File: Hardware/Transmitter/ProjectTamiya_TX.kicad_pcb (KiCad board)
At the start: 2 copper layers, 106.2 x 40 mm, 44 parts, among them J1 Boot, J10 NRF, J11 NRF_power, J2 Power, J3 Serial, J4 Steering, J5 Throttle, J6 ENC1, J7 OLED, J8 ENC2, J9 Debug, Q1 2N7002A, Q2 2N7002A, Q3 2N7002A, SW1 Reset, SW2 Switch, U1 STM32F303CCT6, U2 AP2111H-3.3TRG1, Y1 XT324 [20pF, 12MHz]

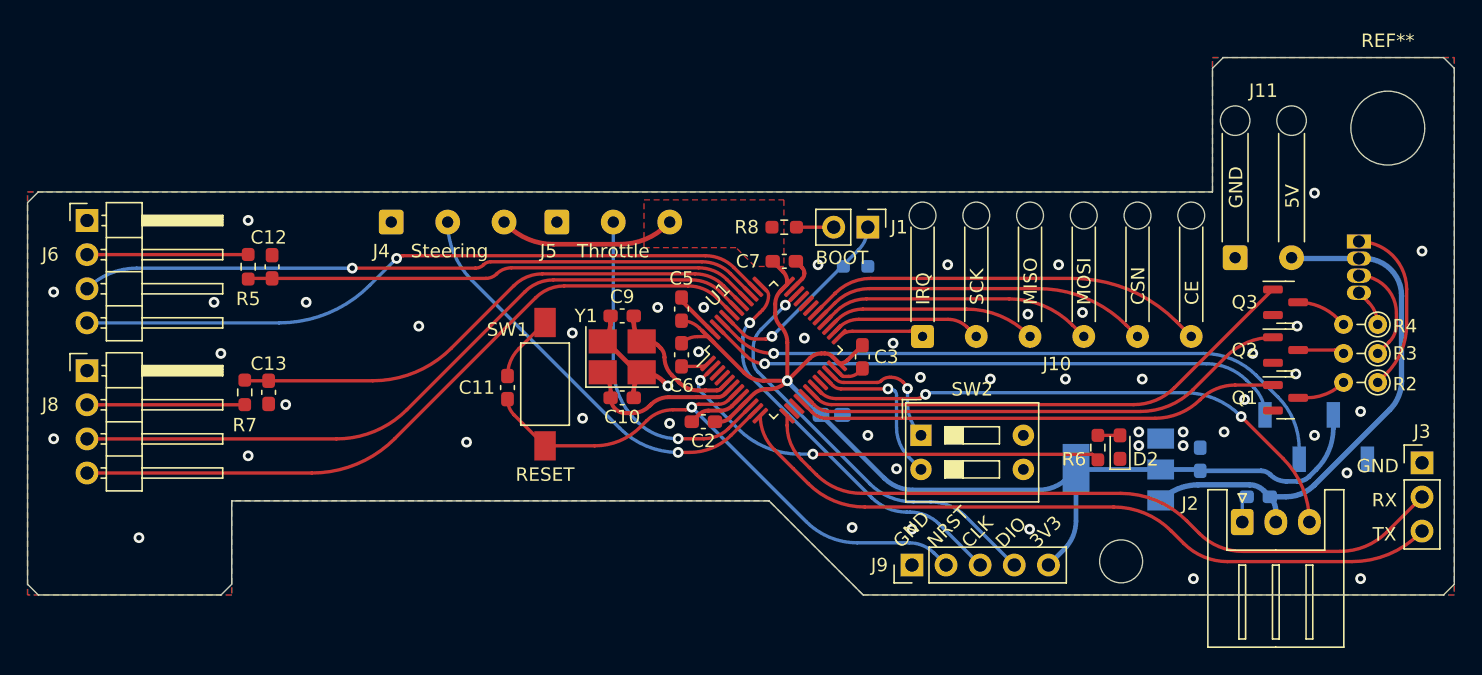
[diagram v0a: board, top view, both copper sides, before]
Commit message: Small PCB routing changes, silkscreen improvements
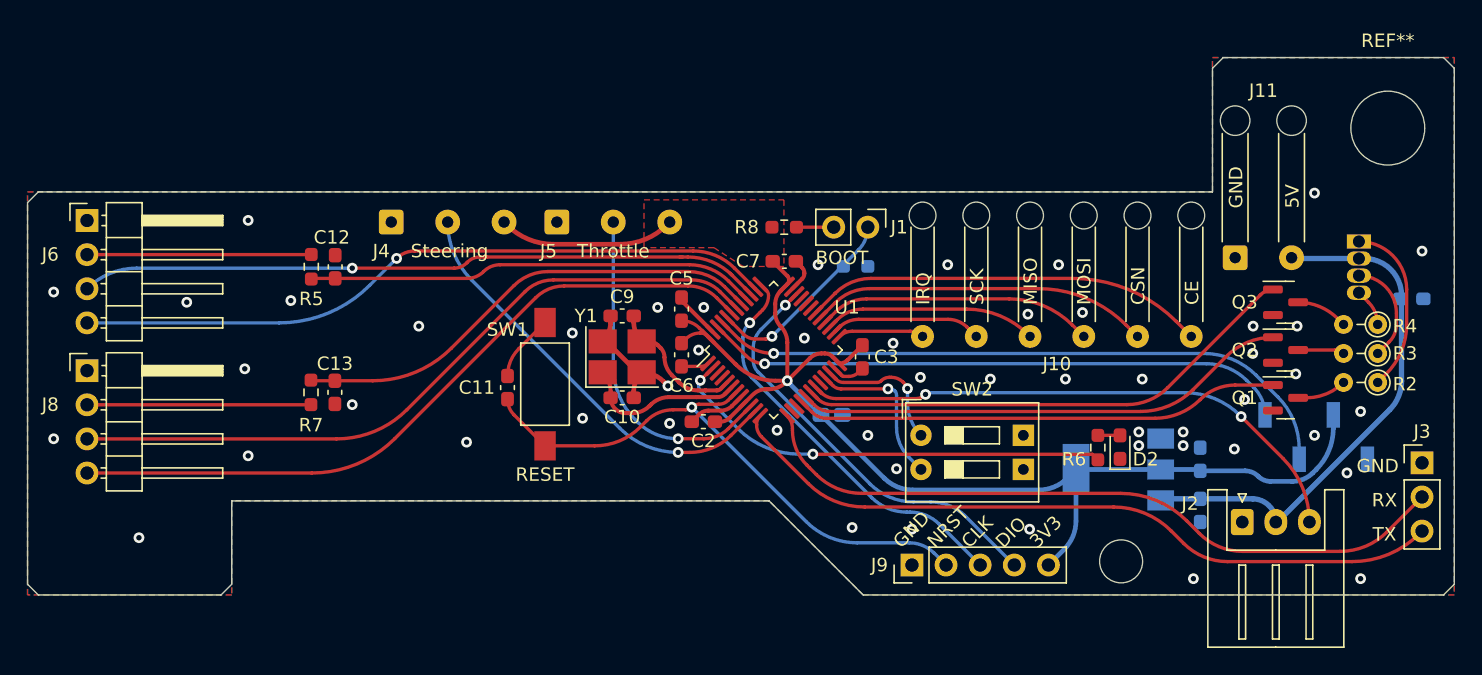
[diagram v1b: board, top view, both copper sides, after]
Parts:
- added C14: 10n, Capacitor_SMD:C_0603_1608Metric_Pad1.08x0.95mm_HandSolder, B.Cu at (161.0, 61.0)
- moved C13 4.93 mm to (80.9, 67.9)
- moved R7 4.93 mm to (79.1, 67.9)
- moved C12 4.70 mm to (80.9, 58.6)
- moved R5 4.70 mm to (79.1, 58.6)
- moved C4 4.44 mm to (145.3, 76.7), turned to -90 degrees
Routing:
- net Net-(J8-Pad2): track 11.7 -> 16.7 mm
- net ENC2_BTN: track 40.5 -> 35.6 mm
- net Net-(J6-Pad2): track 12.0 -> 16.7 mm
- net ENC1_BTN: track 38.1 -> 33.4 mm
- net GND: track 30.2 -> 28.2 mm, vias 50 -> 52
- net +5V: track 40.6 -> 39.8 mm
- net ENC1_CH2: track 50.8 -> 51.3 mm
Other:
- board text added: "ProjectTamiya - TX board v1"

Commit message: Final checkup and small adjustments
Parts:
- moved C14 0.28 mm to (161.2, 60.7)
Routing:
- net GND: vias 52 -> 58

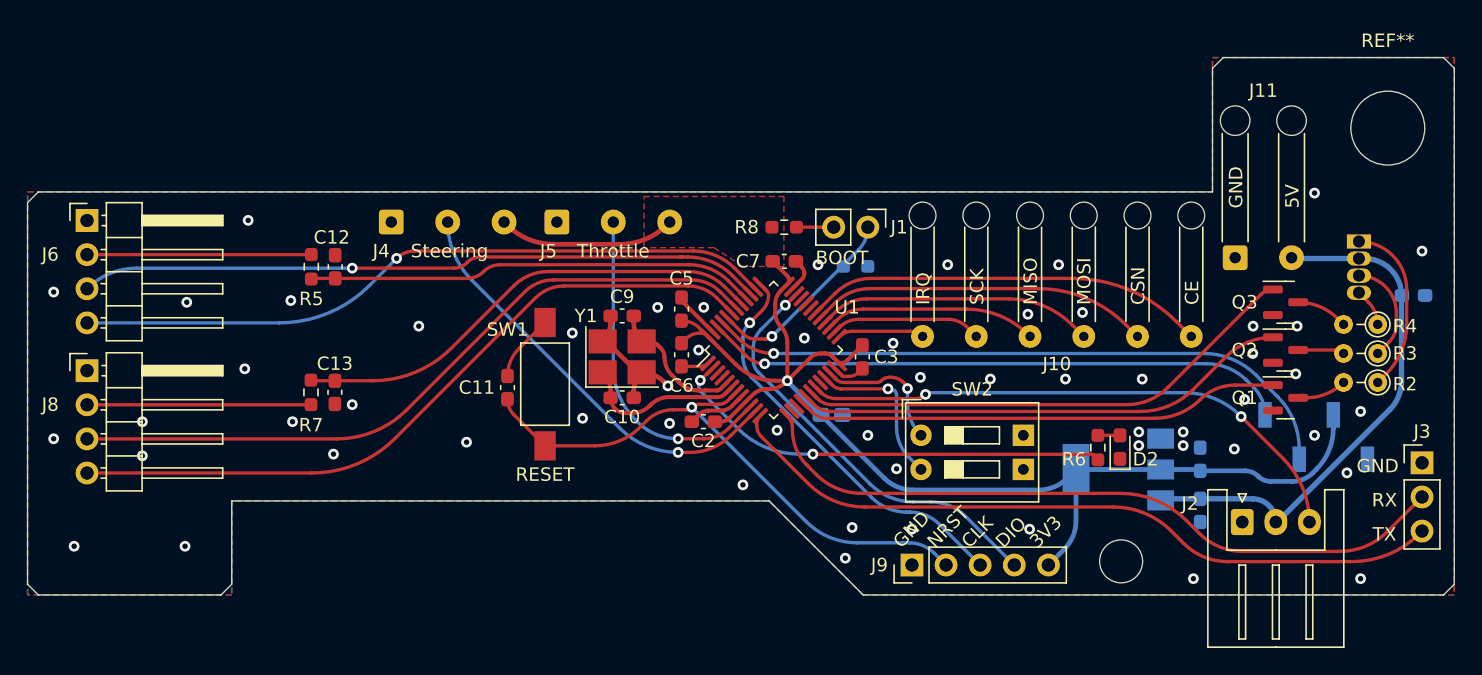
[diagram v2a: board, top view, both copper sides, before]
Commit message: Removed some of the ground vias
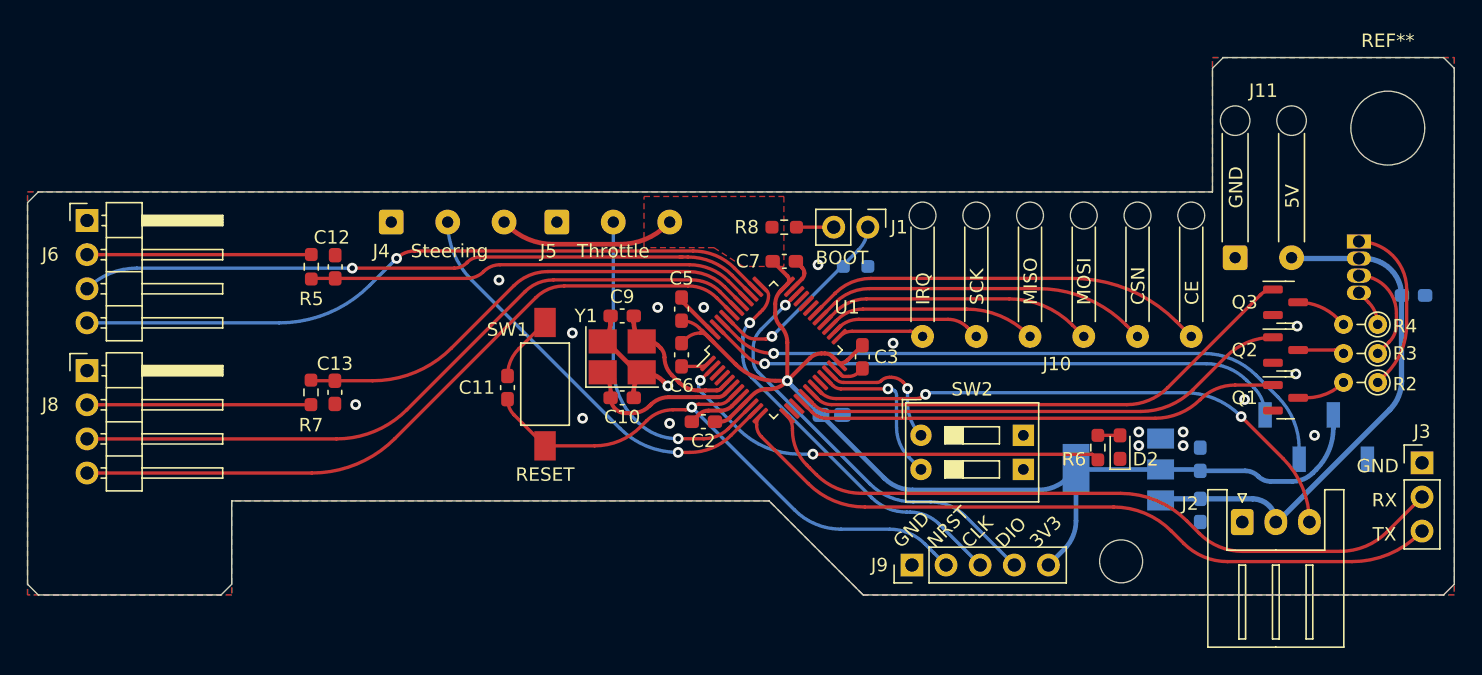
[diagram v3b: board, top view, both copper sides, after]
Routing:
- net GND: vias 58 -> 18
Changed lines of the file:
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@@
   (segment (start 110.440652 68.928008) (end 111.124998 68.243662) (width 0.3) (layer "F.Cu") (net 2))
   (via (at 105.791 70.231) (size 0.8) (drill 0.4) (layers "F.Cu" "B.Cu") (free) (net 2))
-  (via (at 113.792 70.739) (size 0.8) (drill 0.4) (layers "F.Cu" "B.Cu") (free) (net 2))
-  (via (at 80.772 72.517) (size 0.8) (drill 0.4) (layers "F.Cu" "B.Cu") (free) (net 2))
-  (via (at 90.678 71.628) (size 0.8) (drill 0.4) (layers "F.Cu" "B.Cu") (free) (net 2))
   (via (at 140.716 71.882) (size 0.8) (drill 0.4) (layers "F.Cu" "B.Cu") (free) (net 2))
-  (via (at 144.78 81.788) (size 0.8) (drill 0.4) (layers "F.Cu" "B.Cu") (free) (net 2))
-  (via (at 77.724 70.104) (size 0.8) (drill 0.4) (layers "F.Cu" "B.Cu") (free) (net 2))
+  (via (at 93.091 59.563) (size 0.8) (drill 0.4) (layers "F.Cu" "B.Cu") (free) (net 2))
   (via (at 152.4 66.548) (size 0.8) (drill 0.4) (layers "F.Cu" "B.Cu") (free) (net 2))
-  (via (at 135.255 66.929) (size 0.8) (drill 0.4) (layers "F.Cu" "B.Cu") (free) (net 2))
-  (via (at 115.824 63.881) (size 0.8) (drill 0.4) (layers "F.Cu" "B.Cu") (free) (net 2))
-  (via (at 77.597 61.087) (size 0.8) (drill 0.4) (layers "F.Cu" "B.Cu") (free) (net 2))
   (via (at 144.018 70.866) (size 0.8) (drill 0.4) (layers "F.Cu" "B.Cu") (free) (net 2))
   (via (at 122.428 64.262) (size 0.8) (drill 0.4) (layers "F.Cu" "B.Cu") (free) (net 2))
   (via (at 108.331 61.595) (size 0.8) (drill 0.4) (layers "F.Cu" "B.Cu") (free) (net 2))
-  (via (at 132.588 78.105) (size 0.8) (drill 0.4) (layers "F.Cu" "B.Cu") (free) (net 2))
-  (via (at 140.97 66.929) (size 0.8) (drill 0.4) (layers "F.Cu" "B.Cu") (free) (net 2))
-  (via (at 69.85 61.214) (size 0.8) (drill 0.4) (layers "F.Cu" "B.Cu") (free) (net 2))
-  (via (at 61.468 79.375) (size 0.8) (drill 0.4) (layers "F.Cu" "B.Cu") (free) (net 2))
-  (via (at 118.872 80.264) (size 0.8) (drill 0.4) (layers "F.Cu" "B.Cu") (free) (net 2))
   (via (at 116.84 58.42) (size 0.8) (drill 0.4) (layers "F.Cu" "B.Cu") (free) (net 2))
   (via (at 148.59 68.453) (size 0.8) (drill 0.4) (layers "F.Cu" "B.Cu") (free) (net 2))
-  (via (at 107.95 64.77) (size 0.8) (drill 0.4) (layers "F.Cu" "B.Cu") (free) (net 2))
-  (via (at 66.548 70.104) (size 0.8) (drill 0.4) (layers "F.Cu" "B.Cu") (free) (net 2))
   (via (at 153.797 71.12) (size 0.8) (drill 0.4) (layers "F.Cu" "B.Cu") (free) (net 2))
   (via (at 104.902 61.595) (size 0.8) (drill 0.4) (layers "F.Cu" "B.Cu") (free) (net 2))
-  (via (at 59.944 71.374) (size 0.8) (drill 0.4) (layers "F.Cu" "B.Cu") (free) (net 2))
-  (via (at 82.169 68.834) (size 0.8) (drill 0.4) (layers "F.Cu" "B.Cu") (free) (net 2))
+  (via (at 82.423 68.834) (size 0.8) (drill 0.4) (layers "F.Cu" "B.Cu") (free) (net 2))
   (via (at 99.314 69.85) (size 0.8) (drill 0.4) (layers "F.Cu" "B.Cu") (free) (net 2))
   (via (at 98.552 63.5) (size 0.8) (drill 0.4) (layers "F.Cu" "B.Cu") (free) (net 2))
-  (via (at 149.1996 65.024) (size 0.8) (drill 0.4) (layers "F.Cu" "B.Cu") (free) (net 2))
-  (via (at 119.38 77.978) (size 0.8) (drill 0.4) (layers "F.Cu" "B.Cu") (free) (net 2))
-  (via (at 156.21 73.914) (size 0.8) (drill 0.4) (layers "F.Cu" "B.Cu") (free) (net 2))
-  (via (at 153.797 53.086) (size 0.8) (drill 0.4) (layers "F.Cu" "B.Cu") (free) (net 2))
-  (via (at 136.525 61.976) (size 0.8) (drill 0.4) (layers "F.Cu" "B.Cu") (free) (net 2))
-  (via (at 69.723 79.375) (size 0.8) (drill 0.4) (layers "F.Cu" "B.Cu") (free) (net 2))
-  (via (at 59.944 60.452) (size 0.8) (drill 0.4) (layers "F.Cu" "B.Cu") (free) (net 2))
-  (via (at 120.5484 71.12) (size 0.8) (drill 0.4) (layers "F.Cu" "B.Cu") (free) (net 2))
-  (via (at 161.798 57.404) (size 0.8) (drill 0.4) (layers "F.Cu" "B.Cu") (free) (net 2))
-  (via (at 157.226 69.342) (size 0.8) (drill 0.4) (layers "F.Cu" "B.Cu") (free) (net 2))
-  (via (at 129.667 66.929) (size 0.8) (drill 0.4) (layers "F.Cu" "B.Cu") (free) (net 2))
-  (via (at 74.422 55.118) (size 0.8) (drill 0.4) (layers "F.Cu" "B.Cu") (free) (net 2))
   (via (at 105.664 67.437) (size 0.8) (drill 0.4) (layers "F.Cu" "B.Cu") (free) (net 2))
   (via (at 152.5016 62.992) (size 0.8) (drill 0.4) (layers "F.Cu" "B.Cu") (free) (net 2))
-  (via (at 147.828 72.136) (size 0.8) (drill 0.4) (layers "F.Cu" "B.Cu") (free) (net 2))
-  (via (at 123.825 78.105) (size 0.8) (drill 0.4) (layers "F.Cu" "B.Cu") (free) (net 2))
-  (via (at 124.46 66.802) (size 0.8) (drill 0.4) (layers "F.Cu" "B.Cu") (free) (net 2))
-  (via (at 157.226 81.788) (size 0.8) (drill 0.4) (layers "F.Cu" "B.Cu") (free) (net 2))
-  (via (at 132.461 62.103) (size 0.8) (drill 0.4) (layers "F.Cu" "B.Cu") (free) (net 2))
-  (via (at 149.225 62.992) (size 0.8) (drill 0.4) (layers "F.Cu" "B.Cu") (free) (net 2))
-  (via (at 66.548 72.644) (size 0.8) (drill 0.4) (layers "F.Cu" "B.Cu") (free) (net 2))
-  (via (at 134.747 58.42) (size 0.8) (drill 0.4) (layers "F.Cu" "B.Cu") (free) (net 2))
-  (via (at 87.122 62.992) (size 0.8) (drill 0.4) (layers "F.Cu" "B.Cu") (free) (net 2))
-  (via (at 111.252 74.803) (size 0.8) (drill 0.4) (layers "F.Cu" "B.Cu") (free) (net 2))
-  (via (at 126.492 58.42) (size 0.8) (drill 0.4) (layers "F.Cu" "B.Cu") (free) (net 2))
-  (via (at 74.168 66.167) (size 0.8) (drill 0.4) (layers "F.Cu" "B.Cu") (free) (net 2))
   (via (at 140.716 70.866) (size 0.8) (drill 0.4) (layers "F.Cu" "B.Cu") (free) (net 2))
   (via (at 144.018 71.882) (size 0.8) (drill 0.4) (layers "F.Cu" "B.Cu") (free) (net 2))
-  (via (at 122.682 73.6092) (size 0.8) (drill 0.4) (layers "F.Cu" "B.Cu") (free) (net 2))
   (arc (start 115.824 59.055) (mid 115.778605 59.283217) (end 115.64933 59.476689) (width 0.3) (layer "F.Cu") (net 2))
   (arc (start 93.726 66.7015) (mid 93.944228 65.604393) (end 94.565689 64.67431) (width 0.25) (layer "F.Cu") (net 2))
@@
   (arc (start 106.045 69.215) (mid 104.989006 69.42505) (end 104.093777 70.023223) (width 0.25) (layer "F.Cu") (net 7))
   (arc (start 93.726 68.4265) (mid 93.850872 69.054276) (end 94.206479 69.586479) (width 0.25) (layer "F.Cu") (net 7))
-  (segment (start 125.484536 79.886536) (end 126.37 80.772) (width 0.25) (layer "B.Cu") (net 7))
-  (segment (start 119.757261 79.121) (end 123.63637 79.121) (width 0.25) (layer "B.Cu") (net 7))
-  (segment (start 107.442 69.024478) (end 115.969637 77.552115) (width 0.25) (layer "B.Cu") (net 7))
-  (arc (start 115.969637 77.552115) (mid 117.707414 78.71326) (end 119.757261 79.121) (width 0.25) (layer "B.Cu") (net 7))
-  (arc (start 125.476 79.883) (mid 125.48062 79.883919) (end 125.484536 79.886536) (width 0.25) (layer "B.Cu") (net 7))
-  (arc (start 123.63637 79.121) (mid 124.631971 79.319037) (end 125.476 79.883) (width 0.25) (layer "B.Cu") (net 7))
+  (segment (start 126.37 80.772) (end 125.484536 79.886536) (width 0.25) (layer "B.Cu") (net 7))
+  (segment (start 122.174 78.105) (end 118.543095 78.105) (width 0.25) (layer "B.Cu") (net 7))
+  (segment (start 125.476 79.883) (end 124.775631 79.182631) (width 0.25) (layer "B.Cu") (net 7))
+  (segment (start 115.093761 76.676239) (end 107.442 69.024478) (width 0.25) (layer "B.Cu") (net 7))
+  (arc (start 118.543095 78.105) (mid 116.676329 77.733677) (end 115.093761 76.676239) (width 0.25) (layer "B.Cu") (net 7))
+  (arc (start 125.484536 79.886536) (mid 125.48062 79.883919) (end 125.476 79.883) (width 0.25) (layer "B.Cu") (net 7))
+  (arc (start 124.775631 79.182631) (mid 123.581993 78.385067) (end 122.174 78.105) (width 0.25) (layer "B.Cu") (net 7))
   (segment (start 80.899 59.436) (end 90.72158 59.436) (width 0.25) (layer "F.Cu") (net 8))
   (segment (start 110.1725 59.6265) (end 111.471314 60.925314) (width 0.25) (layer "F.Cu") (net 8))

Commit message: Corrected labels to reflect real hardware (DIP switch)
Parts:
- Q1, Q2, Q3: value 2N7002A -> 2N7002BK
- R2: value 220R -> 330R
- R3: value 1K2 -> 5K
- R4: value 680R -> 3K3
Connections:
- J6 pad 3: ENC1_CH2 -> ENC1_CH1
- J6 pad 4: ENC1_CH1 -> ENC1_CH2
- SW2 pad 1: SW1 -> SW2
- SW2 pad 2: SW2 -> SW1
- U1 pad 21: SW2 -> SW1
- U1 pad 22: SW1 -> SW2
- U1 pad 38: ENC1_CH1 -> ENC1_CH2
- U1 pad 39: ENC1_CH2 -> ENC1_CH1
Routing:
- net SW2: track 12.0 -> 10.2 mm
- net SW1: track 10.2 -> 12.0 mm
- net ENC1_CH2: track 50.9 -> 52.4 mm
- net ENC1_CH1: track 52.4 -> 50.9 mm
